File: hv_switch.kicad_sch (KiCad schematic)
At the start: 10 parts, among them IC3 MAX14802CCM+

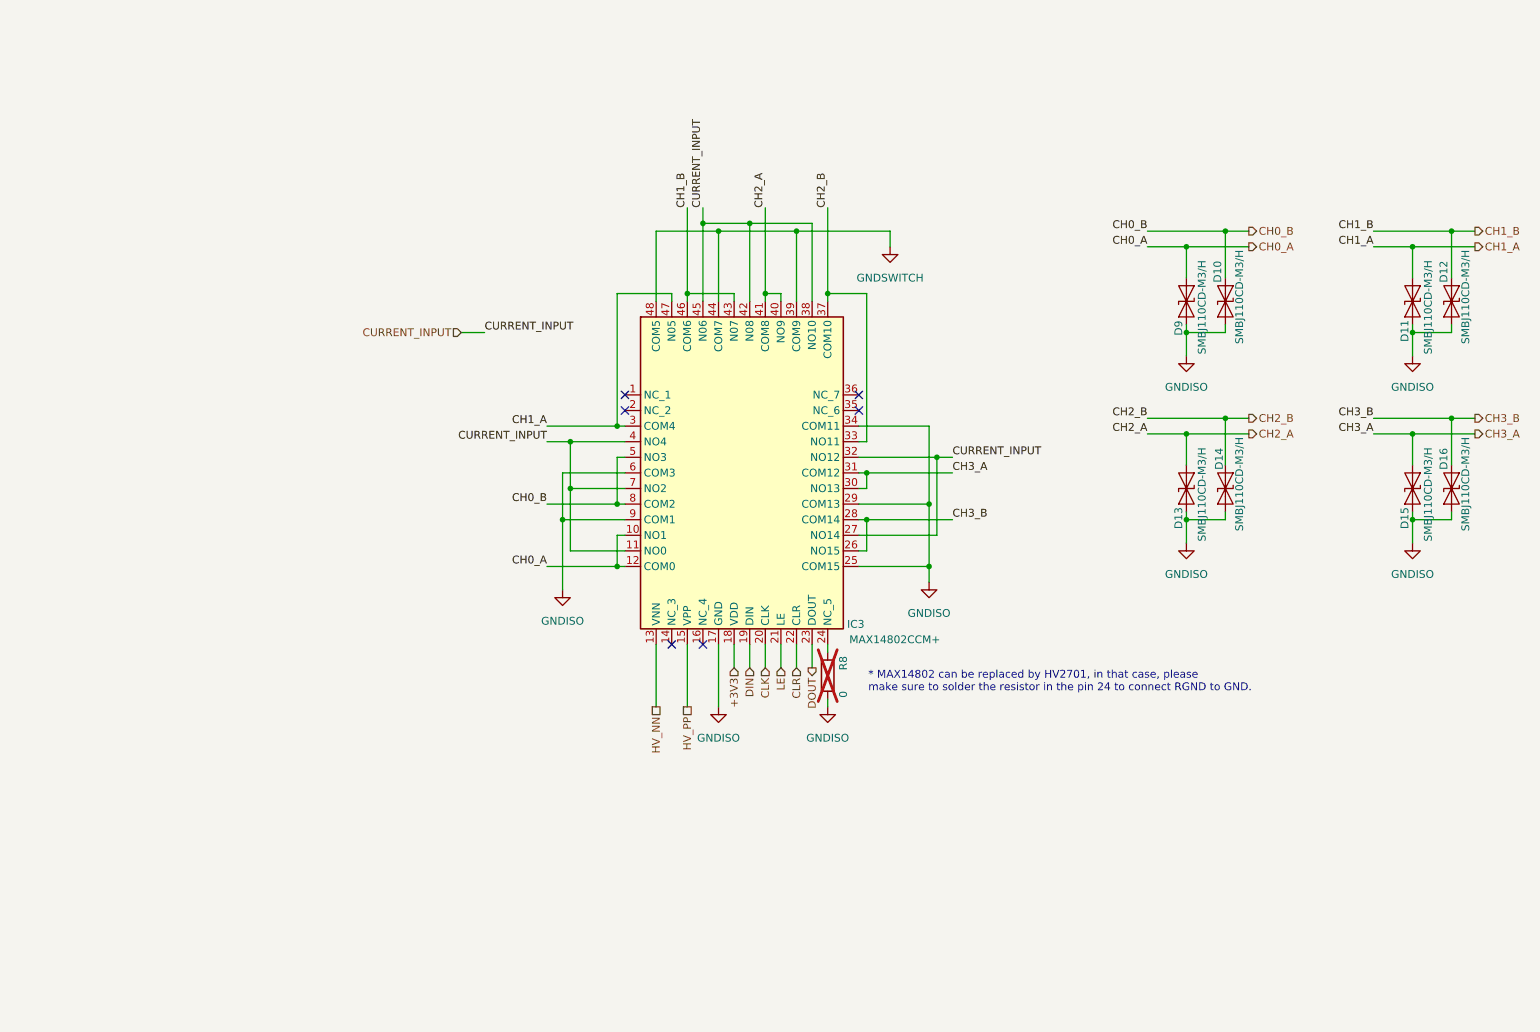
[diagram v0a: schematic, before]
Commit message: fix: replacement of ISO7641 with ISO7640
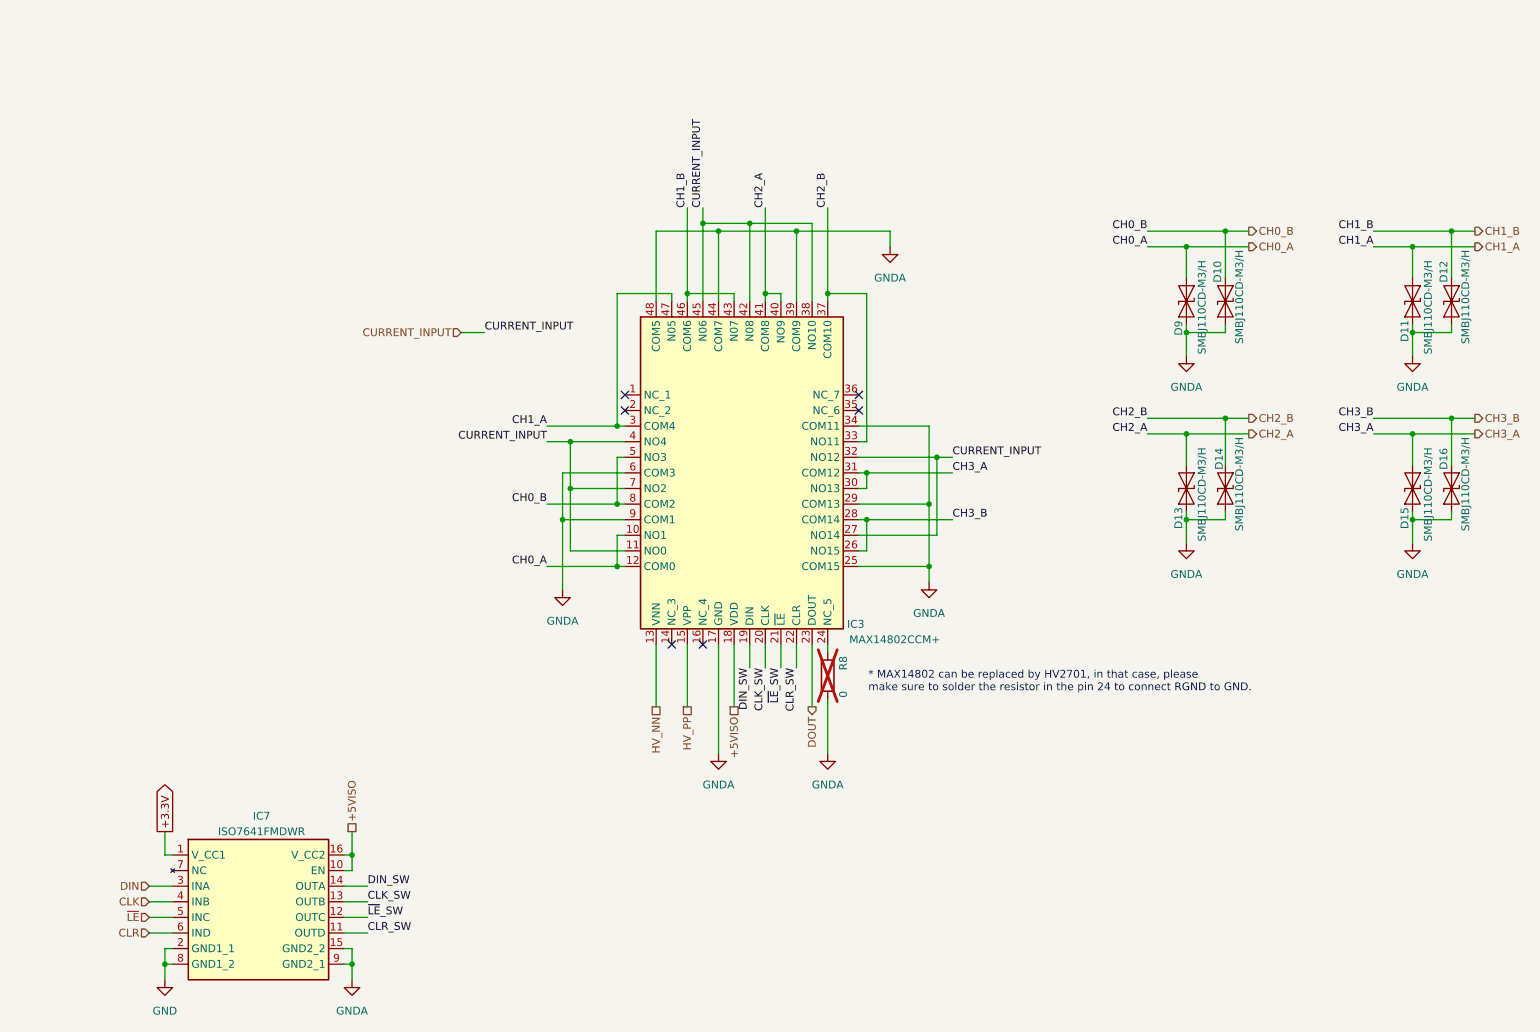
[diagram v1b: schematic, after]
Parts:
- added IC7: ISO7641FMDWR, Package_SO:SOIC-16W_7.5x10.3mm_P1.27mm, symbol Technaid:ISO7640FMDWR
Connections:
- net GNDSWITCH is gone; now on net GNDA: IC3.39 (COM9), IC3.44 (COM7), IC3.48 (COM5)
- net CLK: now also IC7.4 (INB); no longer IC3.20 (CLK)
- net CLR: now also IC7.6 (IND); no longer IC3.22 (CLR)
- net DIN: now also IC7.3 (INA); no longer IC3.19 (DIN)
- net +3V3 renamed +5VISO
- net +5VISO: now also IC7.10 (EN), IC7.16 (V_CC2)
- net GNDISO renamed GNDA
- net GNDA: now also IC7.15 (GND2_2), IC7.9 (GND2_1)
- net LE renamed ~{LE}_SW
- net ~{LE}_SW: now also IC7.12 (OUTC)
- new net +3.3V: IC7.1 (V_CC1)
- new net CLK_SW: IC3.20 (CLK), IC7.13 (OUTB)
- new net CLR_SW: IC3.22 (CLR), IC7.11 (OUTD)
- new net DIN_SW: IC3.19 (DIN), IC7.14 (OUTA)
- new net GND: IC7.2 (GND1_1), IC7.8 (GND1_2)
- new net ~{LE}: IC7.5 (INC)

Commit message: fix: update PCB with last 3dmodels and ICs (ISO7640, GNDISO)
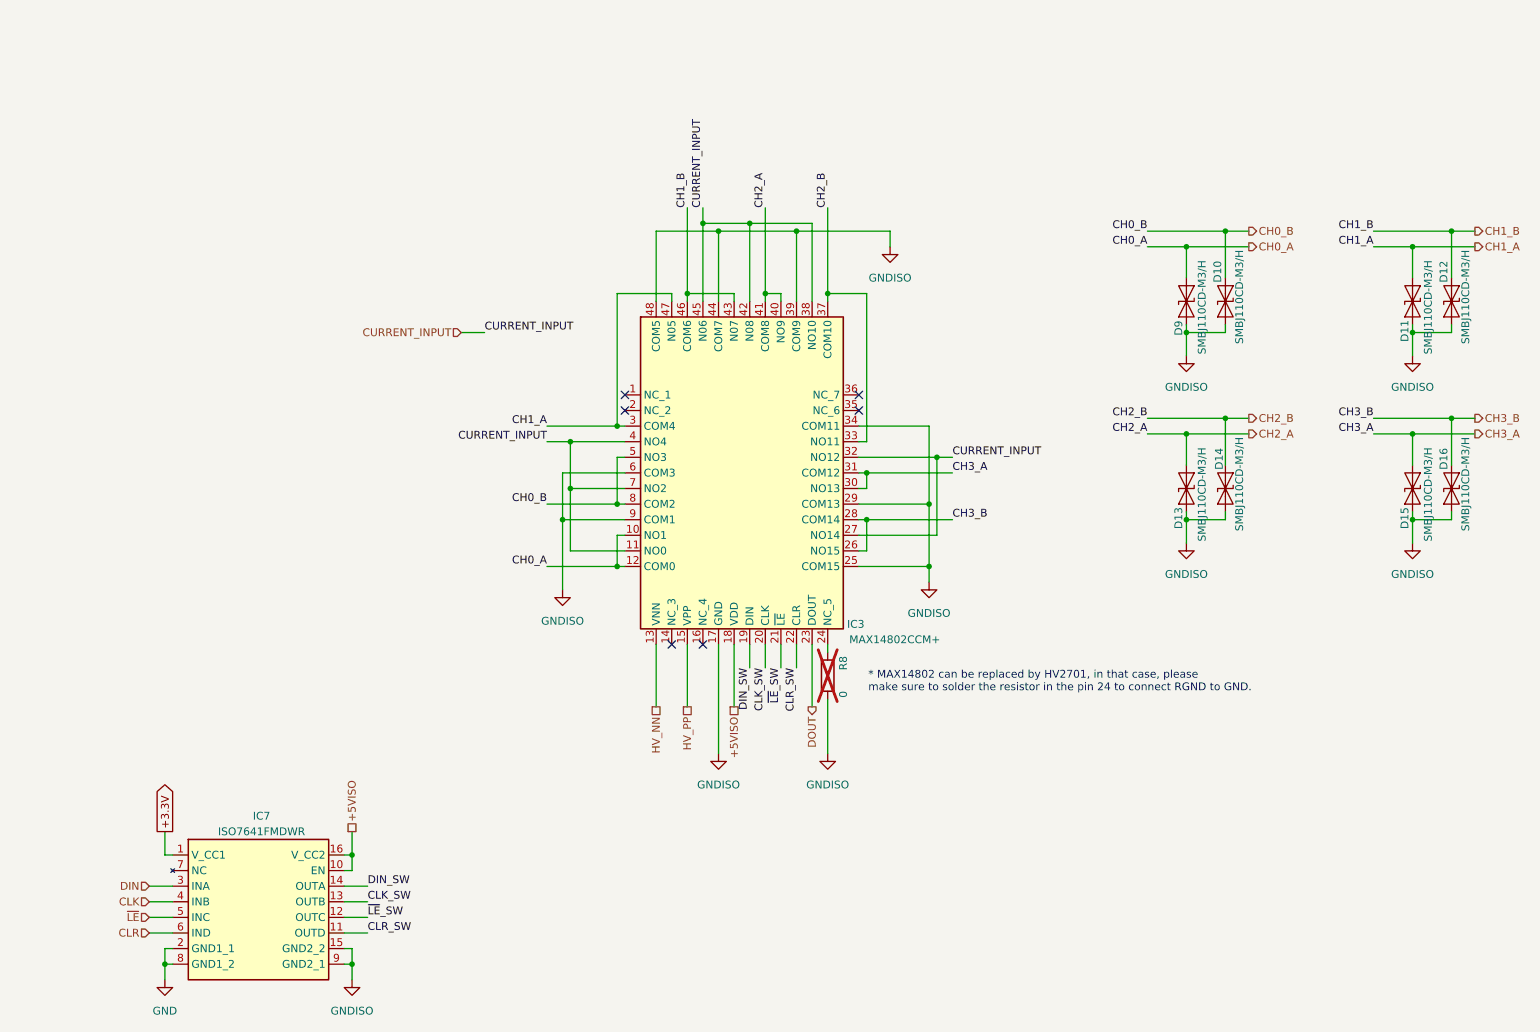
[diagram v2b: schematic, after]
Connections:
- net GNDA renamed GNDISO

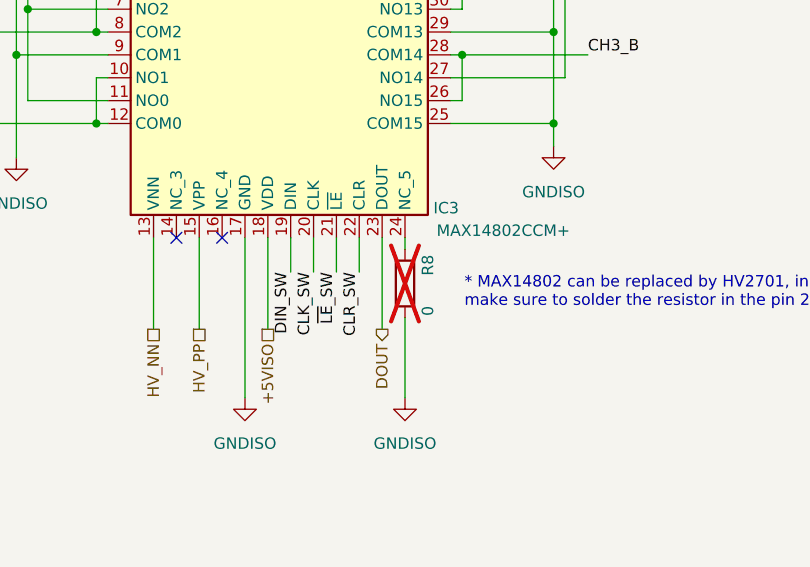
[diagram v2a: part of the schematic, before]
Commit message: docs: update S1L, S1N, MFP, MFN
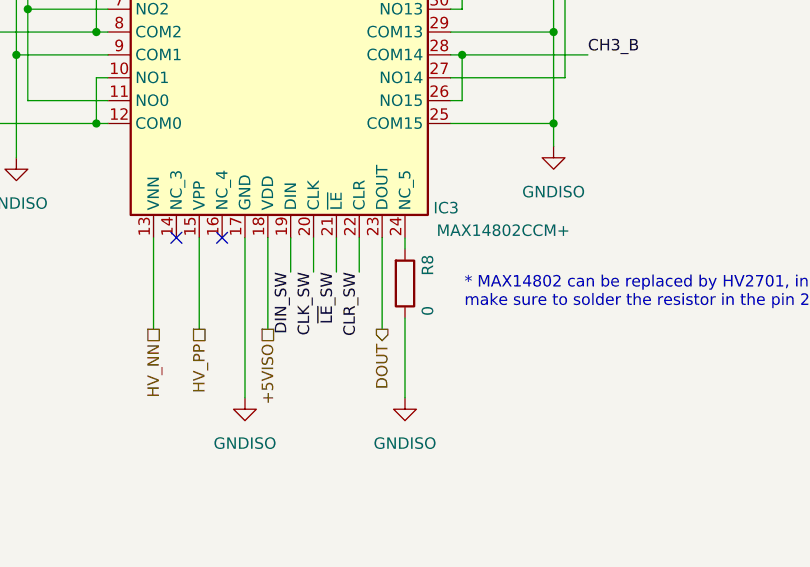
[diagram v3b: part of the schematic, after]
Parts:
- R8: now fitted
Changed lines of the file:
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@@
 		(in_bom yes)
 		(on_board yes)
-		(dnp yes)
+		(dnp no)
 		(property "Reference" "R8"
 			(at 147.32 118.618 90)

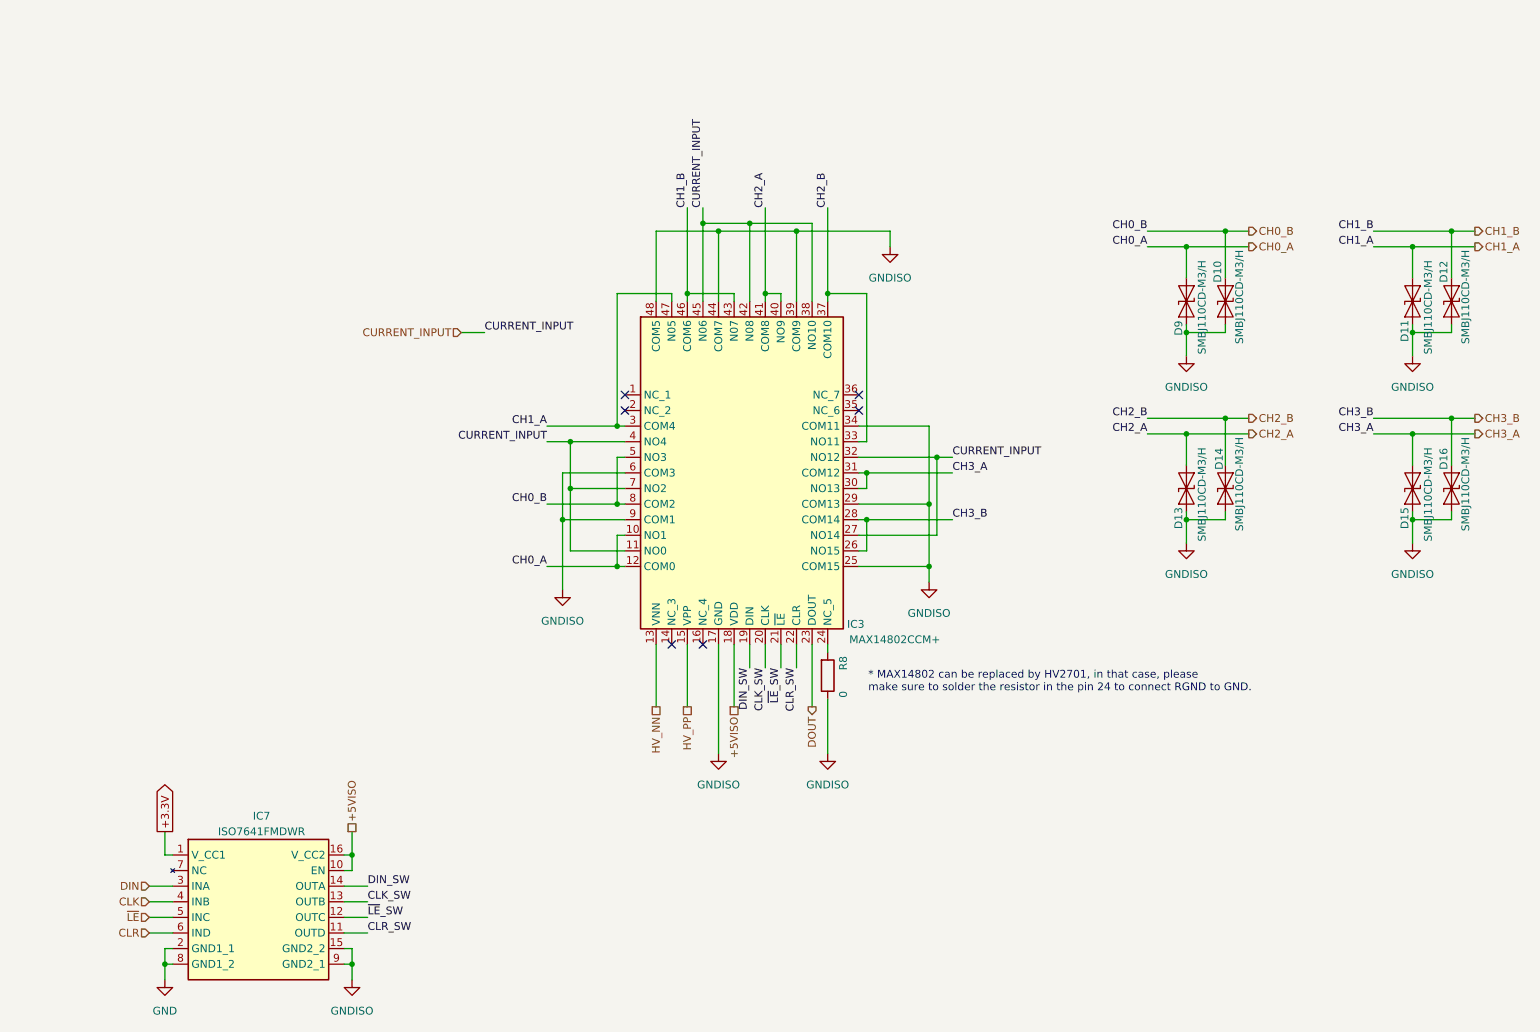
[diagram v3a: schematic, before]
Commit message: fix: adding connector to select communication between HV_Switches
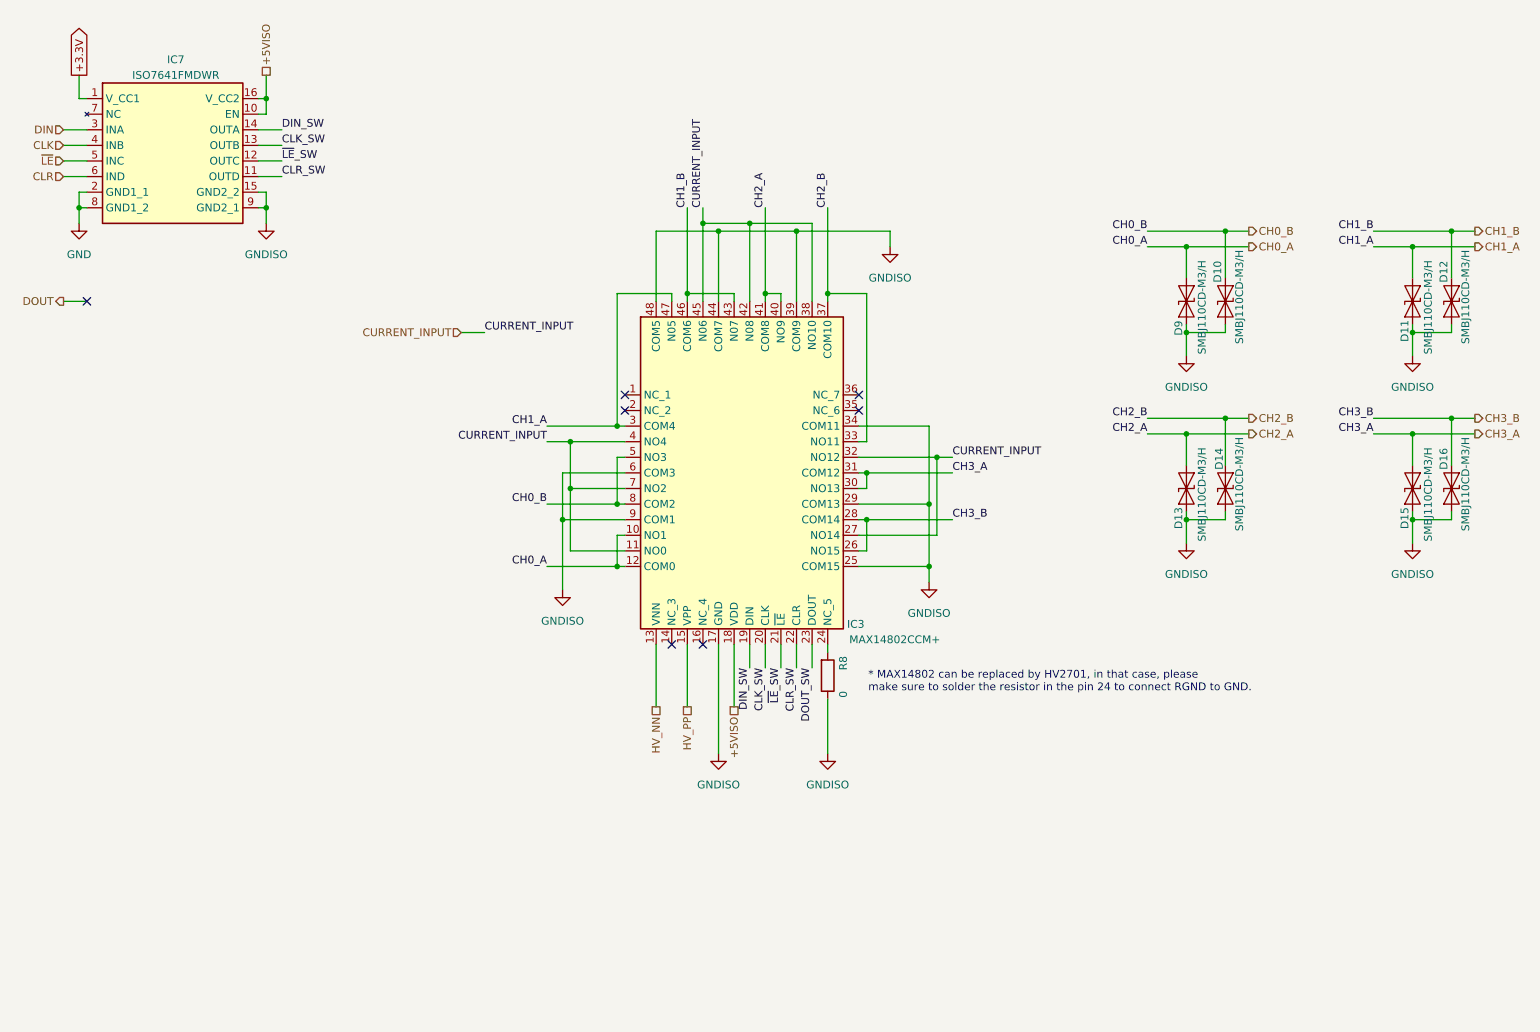
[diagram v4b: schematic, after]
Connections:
- net DOUT: no longer IC3.23 (DOUT)
- new net DOUT_SW: IC3.23 (DOUT)
- no-connect marks 6 -> 7
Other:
- moved on the sheet: IC7

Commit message: ops: adding SP1# field and add all the info for each component
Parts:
- D10, D11, D12, D13, D14, D15, D16, D9: S1P# (none) -> 78-SMBJ110CD-M3/H
- IC3: MFN (none) -> Analog Devices / Maxim Integrated; MFP (none) -> MAX14802CCM+; S1P# (none) -> 700-MAX14802CCM; S1PL (none) -> https://eu.mouser.com/ProductDetail/Analog-Devices-Maxim-In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; S1PN (none) -> Mouser
- IC7: S1P# (none) -> 595-ISO7640FMDWR
- R8: S1P# (none) -> 603-RC0805FR-070RL
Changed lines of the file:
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@@
+			)
+		)
+		(property "S1P#" "78-SMBJ110CD-M3/H "
+			(at 209.55 90.17 0)
+			(effects
+				(font
+					(size 1.27 1.27)
+				)
+				(hide yes)
 			)
 		)
@@
 			)
 		)
+		(property "S1P#" "78-SMBJ110CD-M3/H "
+			(at 246.38 59.69 0)
+			(effects
+				(font
+					(size 1.27 1.27)
+				)
+				(hide yes)
+			)
+		)
 		(pin "2"
 		)
@@
 			)
 		)
+		(property "S1P#" "78-SMBJ110CD-M3/H "
+			(at 203.2 59.69 0)
+			(effects
+				(font
+					(size 1.27 1.27)
+				)
+				(hide yes)
+			)
+		)
 		(pin "2"
 		)
@@
 			)
 		)
+		(property "S1P#" "78-SMBJ110CD-M3/H "
+			(at 246.38 90.17 0)
+			(effects
+				(font
+					(size 1.27 1.27)
+				)
+				(hide yes)
+			)
+		)
 		(pin "2"
 		)
@@
 			)
 		)
+		(property "S1P#" "78-SMBJ110CD-M3/H "
+			(at 240.03 59.69 0)
+			(effects
+				(font
+					(size 1.27 1.27)
+				)
+				(hide yes)
+			)
+		)
 		(pin "2"
 		)
@@
 			)
 		)
+		(property "S1P#" "78-SMBJ110CD-M3/H "
+			(at 209.55 59.69 0)
+			(effects
+				(font
+					(size 1.27 1.27)
+				)
+				(hide yes)
+			)
+		)
 		(pin "2"
 		)
@@
 				)
 				(justify left top)
+				(hide yes)
+			)
+		)
+		(property "MFN" "Analog Devices / Maxim Integrated"
+			(at 114.3 62.23 0)
+			(effects
+				(font
+					(size 1.27 1.27)
+				)
+				(hide yes)
+			)
+		)
+		(property "MFP" "MAX14802CCM+ "
+			(at 114.3 62.23 0)
+			(effects
+				(font
+					(size 1.27 1.27)
+				)
+				(hide yes)
+			)
+		)
+		(property "S1P#" "700-MAX14802CCM"
+			(at 114.3 62.23 0)
+			(effects
+				(font
+					(size 1.27 1.27)
+				)
+				(hide yes)
+			)
+		)
+		(property "S1PL" "https://eu.mouser.com/ProductDetail/Analog-Devices-Maxim-Integrated/MAX14802CCM%2b?qs=LHmEVA8xxfYA%252BG0fCGlljQ%3D%3D"
+			(at 114.3 62.23 0)
+			(effects
+				(font
+					(size 1.27 1.27)
+				)
+				(hide yes)
+			)
+		)
+		(property "S1PN" "Mouser"
+			(at 114.3 62.23 0)
+			(effects
+				(font
+					(size 1.27 1.27)
+				)
 				(hide yes)
 			)
@@
 			)
 		)
+		(property "S1P#" "78-SMBJ110CD-M3/H "
+			(at 203.2 90.17 0)
+			(effects
+				(font
+					(size 1.27 1.27)
+				)
+				(hide yes)
+			)
+		)
 		(pin "2"
 		)
@@
 			)
 		)
+		(property "S1P#" "603-RC0805FR-070RL"
+			(at 144.78 120.65 0)
+			(effects
+				(font
+					(size 1.27 1.27)
+				)
+				(hide yes)
+			)
+		)
 		(pin "2"
 		)
@@
 			)
 		)
+		(property "S1P#" "595-ISO7640FMDWR"
+			(at 21.59 26.67 0)
+			(effects
+				(font
+					(size 1.27 1.27)
+				)
+				(hide yes)
+			)
+		)
 		(pin "10"
 		)
@@
 			(at 240.03 90.17 0)
 			(effects
+				(font
+					(size 1.27 1.27)
+				)
+				(hide yes)
+			)
+		)
+		(property "S1P#" "78-SMBJ110CD-M3/H "
+			(at 240.03 90.17 0)
+			(effects
